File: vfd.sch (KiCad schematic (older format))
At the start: 30 parts, among them Q1 AO3400A, Q2 AO3400A, T1 Wuerth 760390013, U1 SN74AVC8T245PW, U4 MN12864K

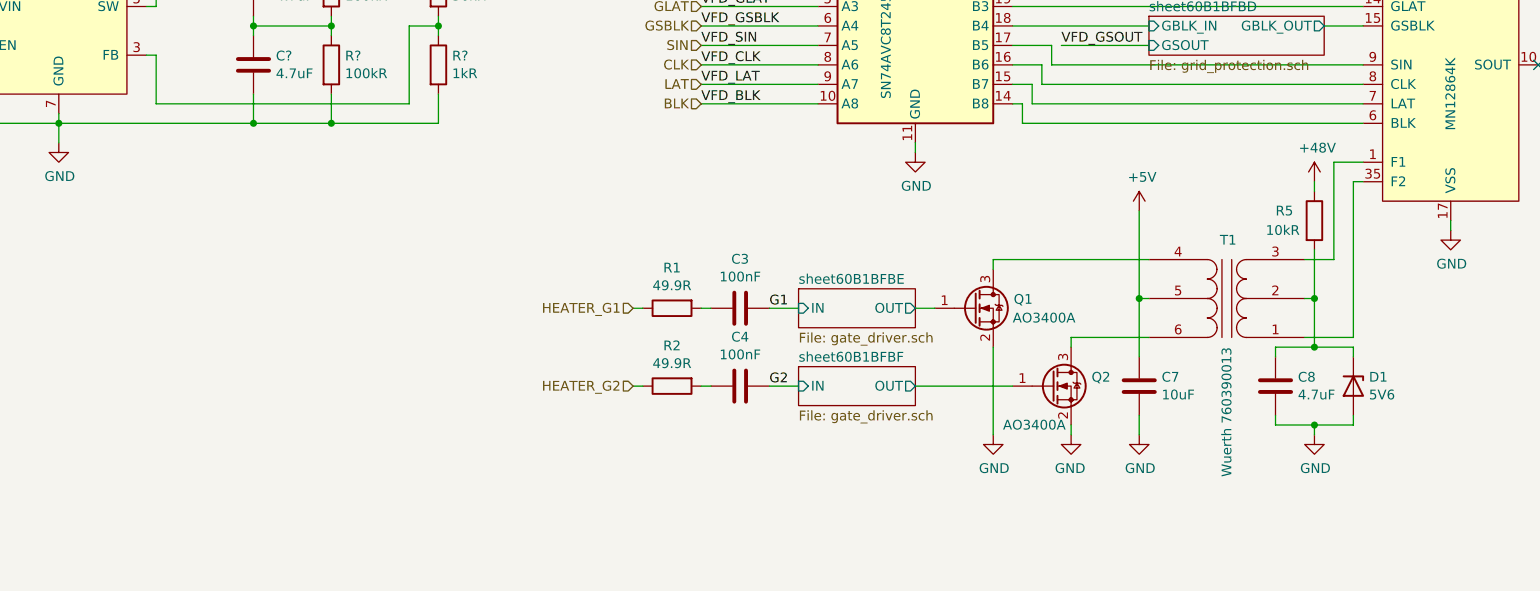
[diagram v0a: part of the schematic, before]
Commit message: Add dual filament transformer option
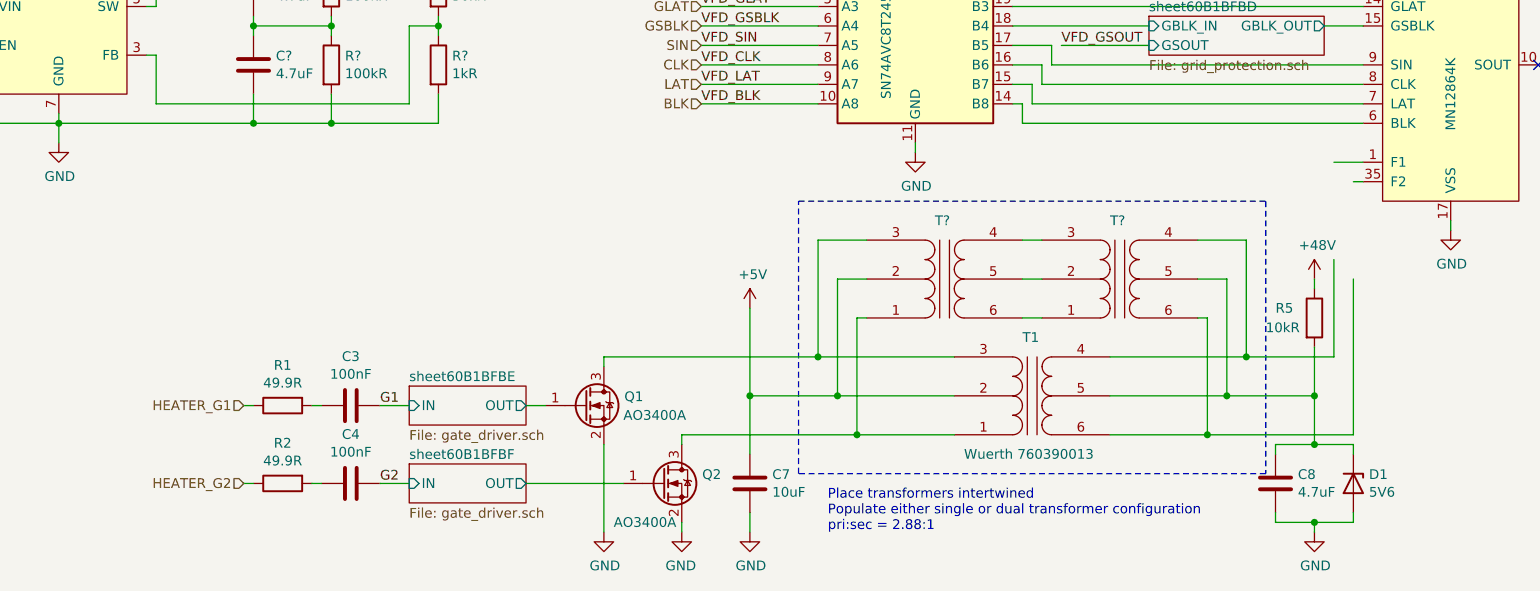
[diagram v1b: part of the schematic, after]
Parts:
- added T? (x2): Wuerth 760390013, Transformer_Würth:Transformer_Würth_10.05x6.73_6P, symbol Transformer_Isolation:Transformer_SP_SS
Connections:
- net +5V: now also T1.2, T?.2; no longer T1.5
- net at U4.1 (F1), U4.2 (F1), U4.3 (F1): no longer T1.3
- net at U4.35 (F2), U4.36 (F1), U4.37 (F1): no longer T1.1
- net at Q2.3 (D): now also T1.1, T?.1; no longer T1.6
- net at Q1.3 (D): now also T1.3, T?.3; no longer T1.4
- net at C8.1, D1.1 (K), R5.2: now also T1.5, T?.5; no longer T1.2
- new net: T1.4, T?.4
- new net: T1.6, T?.6
- new net: T?.3, T?.4
- new net: T?.2, T?.5
- new net: T?.1, T?.6
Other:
- note added: "Place transformers intertwined\nPopulate either single or dual transformer configuration\npri:sec = 2.88:1"
- moved on the sheet: C3, C4, C7, C8, D1, Q1, Q2, R1, R2, R5, T1

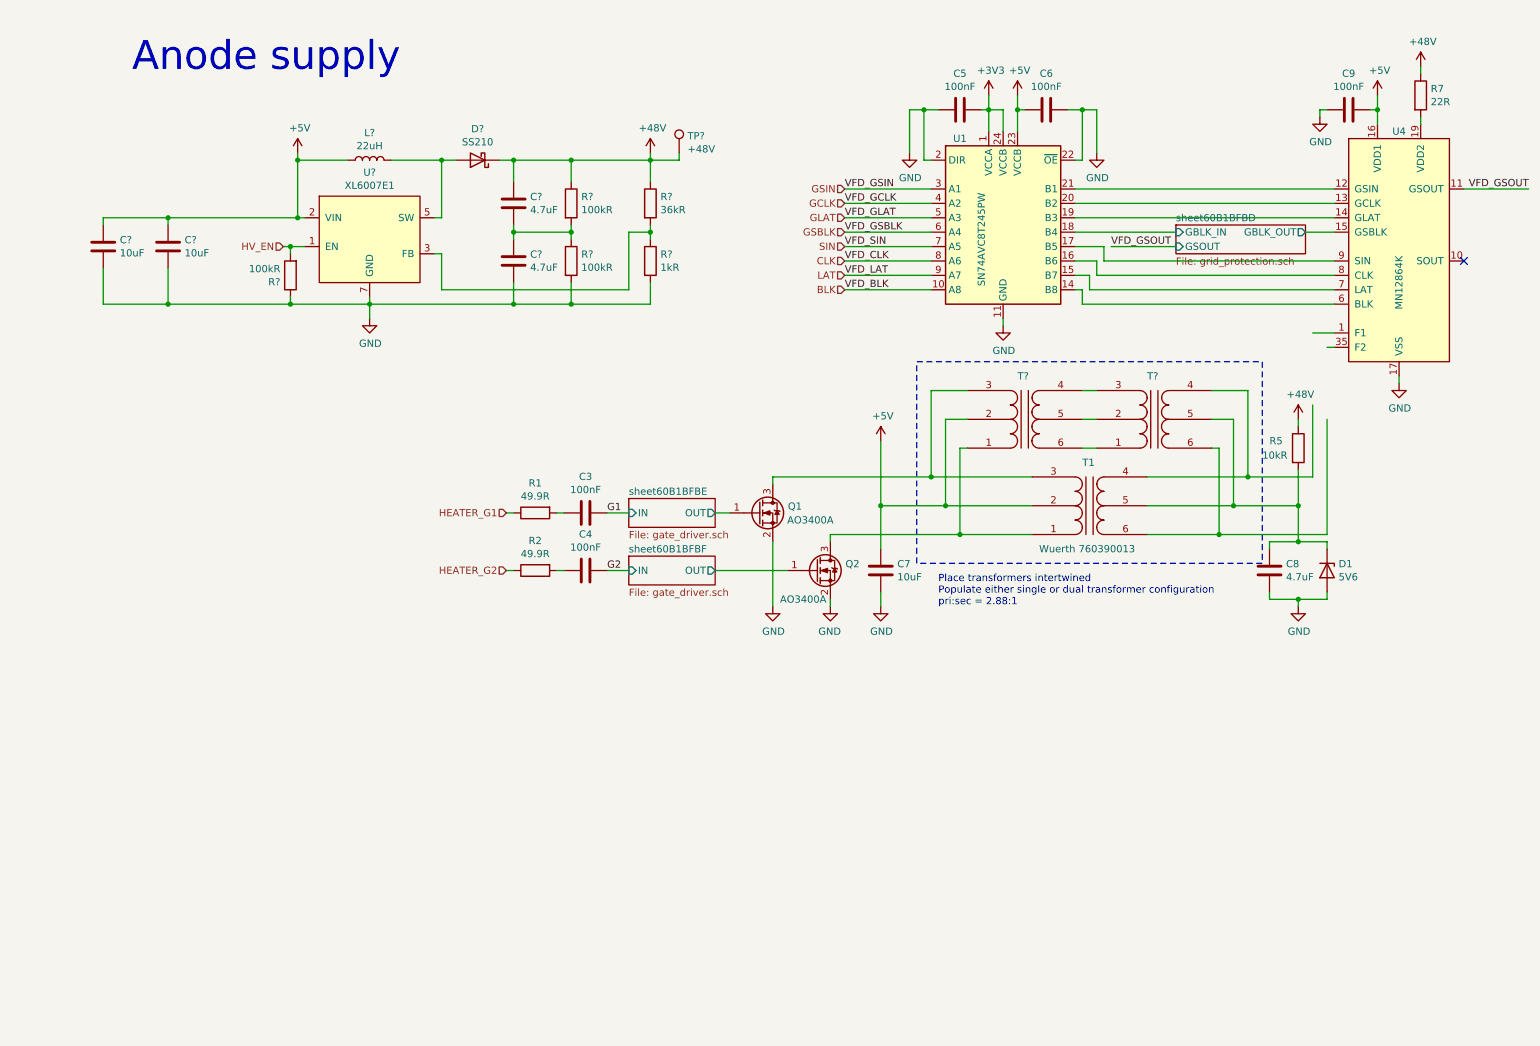
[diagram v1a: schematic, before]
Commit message: Add VFD section
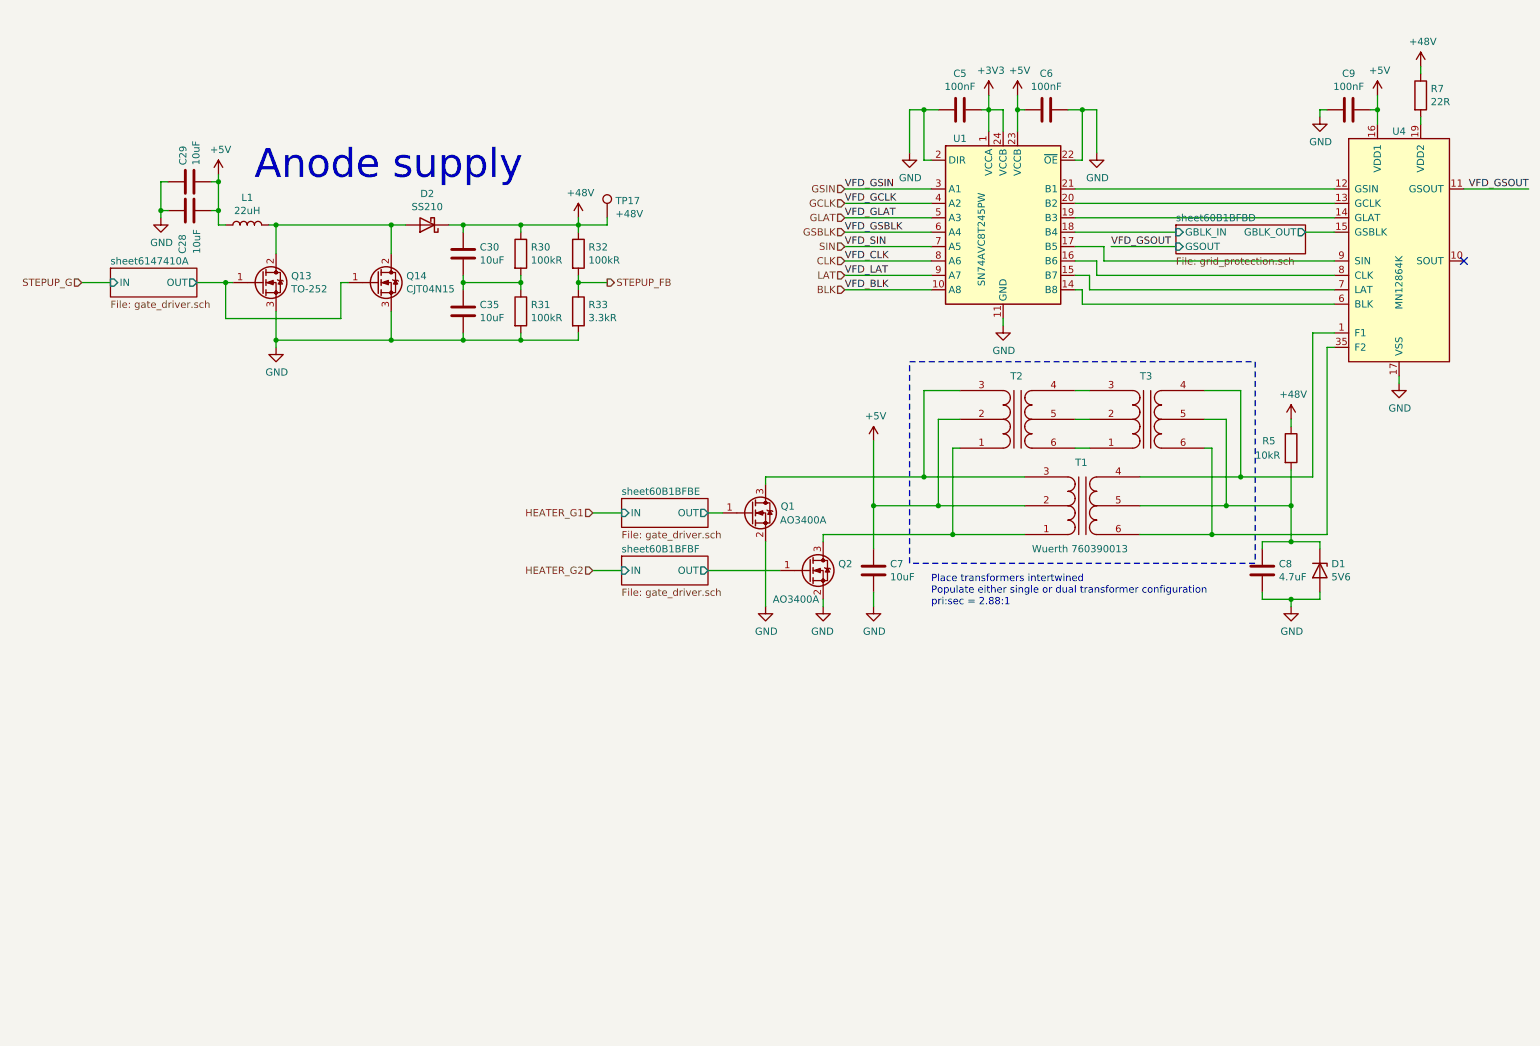
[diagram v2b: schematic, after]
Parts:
- removed C3, C4: 100nF, Capacitor_SMD:C_0402_1005Metric, symbol Device:C
- removed C?: 4.7uF, Capacitor_SMD:C_1206_3216Metric, symbol Device:C
- removed R1, R2: 49.9R, Resistor_SMD:R_0402_1005Metric, symbol Device:R
- removed R?: 36kR, Resistor_SMD:R_0805_2012Metric, symbol Device:R
- removed R?: 100kR, Resistor_SMD:R_0402_1005Metric, symbol Device:R
- removed U?: XL6007E1, Package_SO:SO-8_3.9x4.9mm_P1.27mm, symbol Power_Management_XLSEMI:XL6007E1
- added C35: 10uF, Capacitor_SMD:C_1206_3216Metric, symbol Device:C
- added Q13: TO-252, Package_TO_SOT_SMD:TO-252-3_TabPin2, symbol Device:Q_NMOS_GDS
- added Q14: CJT04N15, Package_TO_SOT_SMD:SOT-223-3_TabPin2, symbol Device:Q_NMOS_GDS
- added R32: 100kR, Resistor_SMD:R_0805_2012Metric, symbol Device:R
- C30: renamed from C?; value 4.7uF -> 10uF; LCSC C29823 -> C13585
- R33: renamed from R?; value 1kR -> 3.3kR; LCSC C11702 -> C25890
- gave numbers to parts that had none: 9
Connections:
- net +48V: now also R32.1
- net +5V: now also C28.2, C29.2; no longer C28.1, C29.1
- net GND: now also C28.1, C29.1, C35.2, Q13.3 (S), Q14.3 (S); no longer C28.2, C29.2
- net at U4.1 (F1), U4.2 (F1), U4.3 (F1): now also T1.4, T3.4
- net at U4.35 (F2), U4.36 (F1), U4.37 (F1): now also T1.6, T3.6
- net STEPUP_FB: now reaches R33.1
- net STEPUP_FB: now also R32.2
- net at D2.2 (A), L1.2: now also Q13.2 (D), Q14.2 (D)
- net at C30.2, R30.2, R31.1: now also C35.1
- new net sheet6147410A/OUT: Q13.1 (G), Q14.1 (G)
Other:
- moved on the sheet: C28, C29, C30, C7, C8, D1, D2, L1, Q1, Q2, R30, R31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

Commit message: Complete intra section layout
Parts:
- R7: footprint Resistor_SMD:R_1206_3216Metric -> Resistor_SMD:R_0805_2012Metric; LCSC C17958 -> C17561
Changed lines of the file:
@@
 F 0 "R7" H 10370 1146 50  0000 L CNN
 F 1 "22R" H 10370 1055 50  0000 L CNN
-F 2 "Resistor_SMD:R_1206_3216Metric" V 10230 1100 50  0001 C CNN
+F 2 "Resistor_SMD:R_0805_2012Metric" V 10230 1100 50  0001 C CNN
 F 3 "~" H 10300 1100 50  0001 C CNN
-F 4 "C17958" H 10300 1100 50  0001 C CNN "LCSC"
+F 4 "C17561" H 10300 1100 50  0001 C CNN "LCSC"
 	1    10300 1100
 	1    0    0    -1

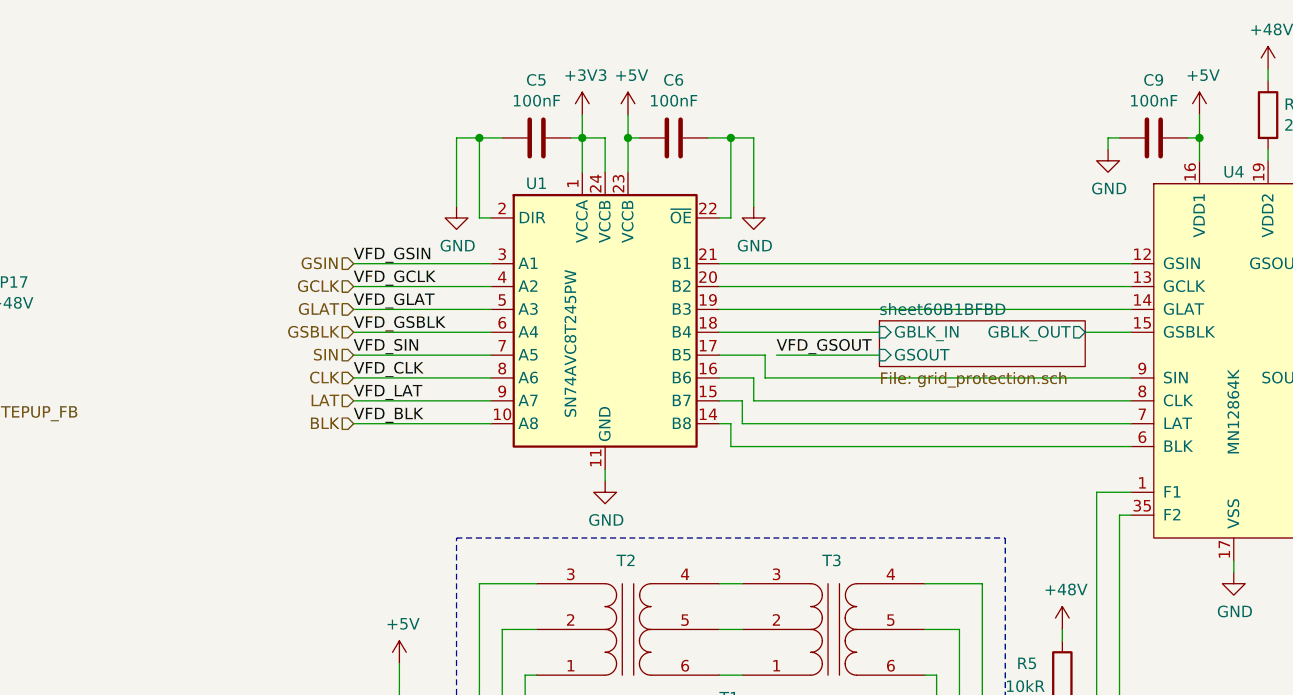
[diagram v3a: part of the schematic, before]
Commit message: Fix level shifter
Level shifter was flipped in scheatic
Pressed "y" one too many times on that thing :/
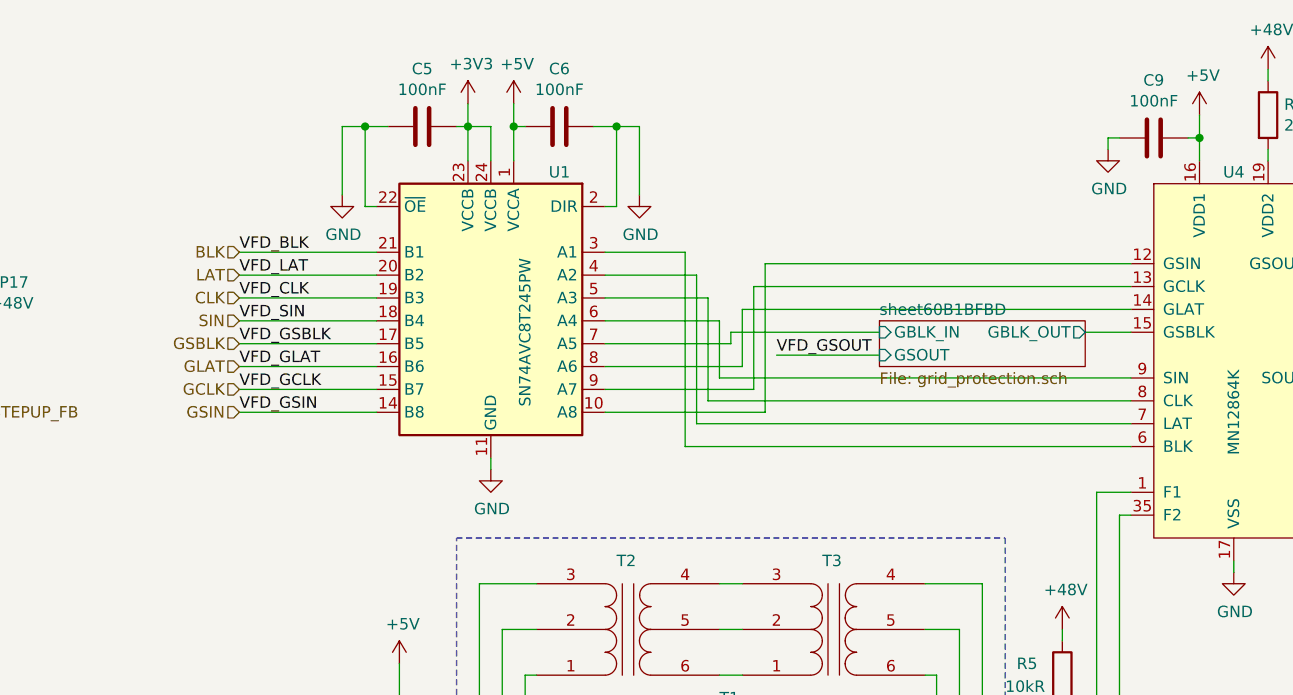
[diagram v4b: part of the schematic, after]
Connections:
- net +3V3: now also U1.23 (VCCB); no longer U1.1 (VCCA)
- net +5V: now also U1.1 (VCCA); no longer U1.23 (VCCB)
- net BLK: now also U1.21 (B1); no longer U1.10 (A8)
- net CLK: now also U1.19 (B3); no longer U1.8 (A6)
- net GCLK: now also U1.15 (B7); no longer U1.4 (A2)
- net GLAT: now also U1.16 (B6); no longer U1.5 (A3)
- net GSBLK: now also U1.17 (B5); no longer U1.6 (A4)
- net GSIN: now also U1.14 (B8); no longer U1.3 (A1)
- net LAT: now also U1.20 (B2); no longer U1.9 (A7)
- net SIN: now also U1.18 (B4); no longer U1.7 (A5)
- net sheet60B1BFBD/GBLK_IN: now also U1.7 (A5); no longer U1.18 (B4)
- net at U4.12 (GSIN): now also U1.10 (A8); no longer U1.21 (B1)
- net at U4.13 (GCLK): now also U1.9 (A7); no longer U1.20 (B2)
- net at U4.14 (GLAT): now also U1.8 (A6); no longer U1.19 (B3)
- net at U4.6 (BLK): now also U1.3 (A1); no longer U1.14 (B8)
- net at U4.7 (LAT): now also U1.4 (A2); no longer U1.15 (B7)
- net at U4.8 (CLK): now also U1.5 (A3); no longer U1.16 (B6)
- net at U4.9 (SIN): now also U1.6 (A4); no longer U1.17 (B5)
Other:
- moved on the sheet: C5, C6, U1
